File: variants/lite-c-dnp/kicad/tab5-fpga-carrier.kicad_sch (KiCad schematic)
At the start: 116 parts, among them J1 DC 12V ONLY, J2 USB-C PD in, J3 M5-BUS (to Tab5), J4 SOCKET XDAP-4042044-20401, J5 HDMI OUT, J6 PMOD1, J7 PMOD2, J8 GPIO pads, Q1 2N7002, Q2 2N7002, Q3 2N7002, Q4 2N7002, SW1 SW, SW2 RESET (Tab5), SW3 FPGA ON/OFF, U1 CH224K, U10 TPS3839K50DBZR, U2 TPS5430DDAR, U3 XC6206P332MR-G, U4 RCLAMP0524P, U5 RCLAMP0524P, U6 SRV05-4, U7 SN74CB3Q3245PWR, U8 SN74CB3Q3245PWR, U9 TPS3839G33DBZR

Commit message: Qualify lite variants for conditional PoC fabrication and publish per-board reports
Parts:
- removed U6: SRV05-4, Package_TO_SOT_SMD:SOT-23-6, symbol Power_Protection:SRV05-4
- added C24: 100n, Capacitor_SMD:C_0603_1608Metric, symbol Device:C
- added Q5: MMBT3904, Package_TO_SOT_SMD:SOT-23, symbol Transistor_BJT:MMBT3904
- added R51: 47k, Resistor_SMD:R_0603_1608Metric, symbol Device:R
- added R52: 10k, Resistor_SMD:R_0603_1608Metric, symbol Device:R
- added U6: RCLAMP0524P, carrier:DFN2510-10L_RCLAMP0524P, symbol carrier:RCLAMP0524P
- C12, C13, C14, C15, C16, C17, C18, C19: footprint Capacitor_SMD:C_0603_1608Metric -> Capacitor_SMD:C_0402_1005Metric; Comment LITE-C DNP: retain circuit/lands; -> 100nF AC coupling; low-profile 0402 under Core; LCSC C14663 -> C1525
- C2, F2, Q2, R1, R2, R28, R29, R30, R31, R32, R33, R34, R35, R36, R37, R38, R39: Comment LITE-C DNP: retain circuit/lands; -> LITE-C DNP: retain circuit/lands;
- R10, R11, R12, R13, R14, R15, R16, R19, R20, R21, R22, R23, R24, R26, R27: value 33R -> 680R; Comment (none) -> PoC 1MHz, 680ohm series damping; >=250ns DATA setup/hold, w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; LCSC C23140 -> C23228
- R40: value 10k -> 47k; Comment LITE-C DNP: retain circuit/lands; -> LITE-C DNP: retain circuit/lands;; LCSC C25804 -> C25819
- R41: value 20k -> 100k; Comment LITE-C DNP: retain circuit/lands; -> LITE-C DNP: retain circuit/lands;; LCSC C4184 -> C25803
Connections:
- net +3V3: now also R51.1
- net F_HPD: now also R52.2; no longer R40.2, R41.1
- net GND: now also C24.2, Q5.2 (E), U6.3 (GND), U6.8 (GND)
- net HDMI_5V: now also U6.2 (IO2), U6.9 (NC)
- net HDMI_HPD: now also U6.5 (IO4), U6.6 (NC)
- net HDMI_SCL: now also U6.4 (IO3), U6.7 (NC)
- net HDMI_SDA: now also U6.1 (IO1), U6.10 (NC)
- new net HPD_B: Q5.1 (B), R40.2, R41.1
- new net HPD_BUF: C24.1, Q5.3 (C), R51.2, R52.1
- no-connect marks 13 -> 12

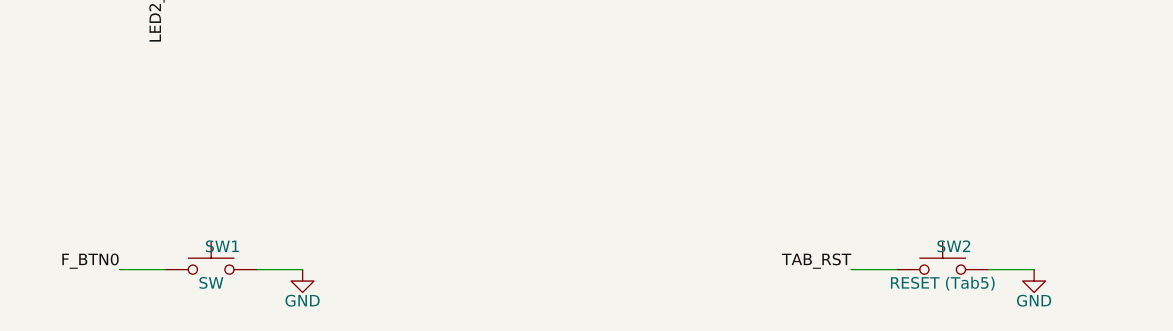
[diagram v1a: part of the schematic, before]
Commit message: Align variants B and C with Akizuki buttons and explain A BOM
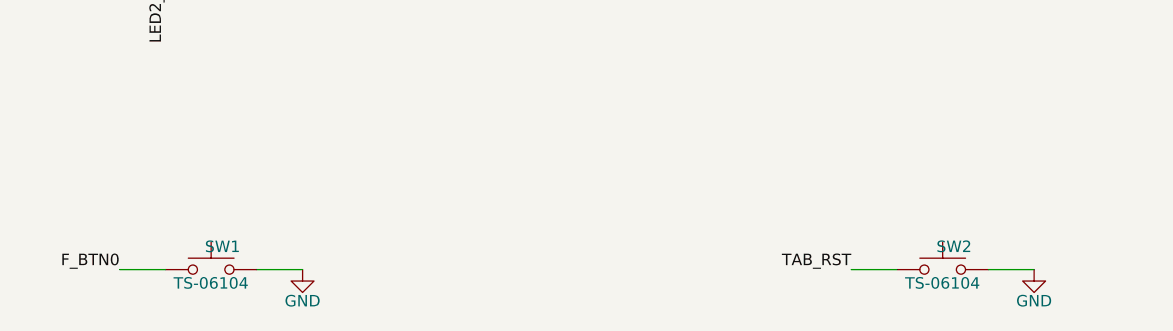
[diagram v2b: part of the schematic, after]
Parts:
- SW1: value SW -> TS-06104; footprint Button_Switch_SMD:SW_SPST_EVQP0 -> carrier:SW_TS_06104_HandSolder; Comment (none) -> Manual assembly; Akizuki115969; TS-06104 H4.3mm; dedicated 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
- SW2: value RESET (Tab5) -> TS-06104; footprint Button_Switch_SMD:SW_SPST_EVQP0 -> carrier:SW_TS_06104_HandSolder; Comment pulls the M5-Bus RST/EN line (pin 6) low: resets the ESP32-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 -> Manual assembly; Akizuki115969; TS-06104 H4.3mm; dedicated 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
